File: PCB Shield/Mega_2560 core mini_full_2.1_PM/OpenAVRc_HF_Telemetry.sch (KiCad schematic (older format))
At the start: 14 parts, among them P18 Ecolage, P19 Module_TX, P20 TTL/RS232, P3 FTDI, P7 SPIX, U1 74LVC1G3157GV, U2 74LVC1G3157GV, U3 74LVC1G3157GV

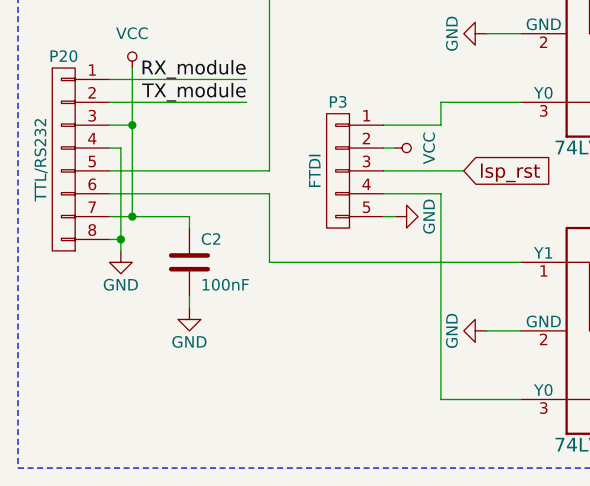
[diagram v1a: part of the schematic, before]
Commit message: Update schematic & pcb files
- modify pcb for haptic.
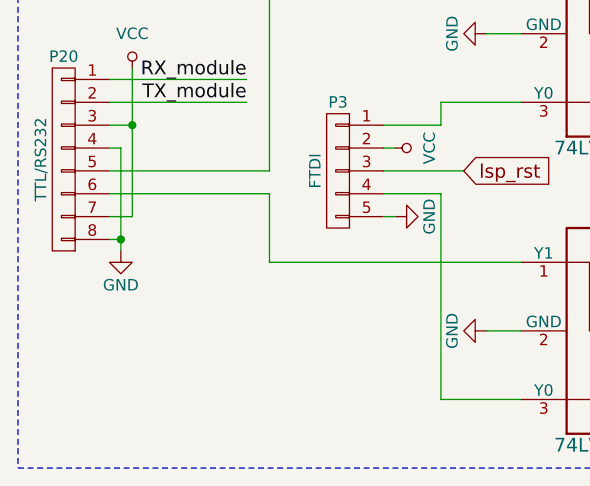
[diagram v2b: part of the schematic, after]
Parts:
- removed C2: 100nF, Capacitors_SMD:C_1206, symbol C-RESCUE-Mega_2560_core_mini_full_2.0
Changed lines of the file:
@@
 Sheet 4 7
 Title "Shield Mega2560 core Full"
-Date "2018-03-01"
+Date "2018-03-02"
 Rev "2.10"
 Comp "© Team OpenAVRc"
@@
 Wire Notes Line
 	4400 800  3250 800
-Wire Wire Line
-	1100 5200 1450 5200
 Wire Wire Line
 	1150 5300 1100 5300
@@
 Wire Wire Line
 	1800 5100 1100 5100
-$Comp
-L C-RESCUE-Mega_2560_core_mini_full_2.0 C2
-U 1 1 5A92C79D
-P 1450 5400
-F 0 "C2" H 1500 5500 50  0000 L CNN
-F 1 "100nF" H 1500 5300 50  0000 L CNN
-F 2 "Capacitors_SMD:C_1206" H 1488 5250 50  0001 C CNN
-F 3 "" H 1450 5400 50  0000 C CNN
-	1    1450 5400
-	1    0    0    -1
-$EndComp
-$Comp
-L GND-RESCUE-Mega_2560_core_mini_full_2.0 #PWR085
-U 1 1 5A92C7A3
-P 1450 5600
-F 0 "#PWR085" H 1450 5350 50  0001 C CNN
-F 1 "GND" H 1450 5450 50  0000 C CNN
-F 2 "" H 1450 5600 50  0000 C CNN
-F 3 "" H 1450 5600 50  0000 C CNN
-	1    1450 5600
-	1    0    0    -1
-$EndComp
-Wire Wire Line
-	1450 5600 1450 5550
-Wire Wire Line
-	1450 5200 1450 5250
-Connection ~ 1200 5200
 Wire Wire Line
 	2550 4700 2550 4800
@@
 Wire Wire Line
 	2900 5700 2750 5700
+Wire Wire Line
+	1200 5200 1100 5200
 $EndSCHEMATC

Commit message: Update schematic & pcb files
-remove P27.
-clean hold_power signal.
-add G3,H7 and G4 pins as dummy pins on 3 pins connector.
-update schematic.
-remove package errors in pcbnew.
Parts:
- P3: footprint (none) -> Pin_Header_Straight_1x05_Pitch2.54mm
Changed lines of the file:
@@
 Sheet 4 7
 Title "Shield Mega2560 core Full"
-Date "2018-03-02"
+Date "2018-03-06"
 Rev "2.10"
 Comp "© Team OpenAVRc"
@@
 F 0 "P3" H 2100 5300 50  0000 C CNN
 F 1 "FTDI" V 2200 5000 50  0000 C CNN
-F 2 "" H 2100 5000 50  0000 C CNN
+F 2 "Pin_Header_Straight_1x05_Pitch2.54mm" H 2100 5000 50  0001 C CNN
 F 3 "" H 2100 5000 50  0000 C CNN
 	1    2100 5000

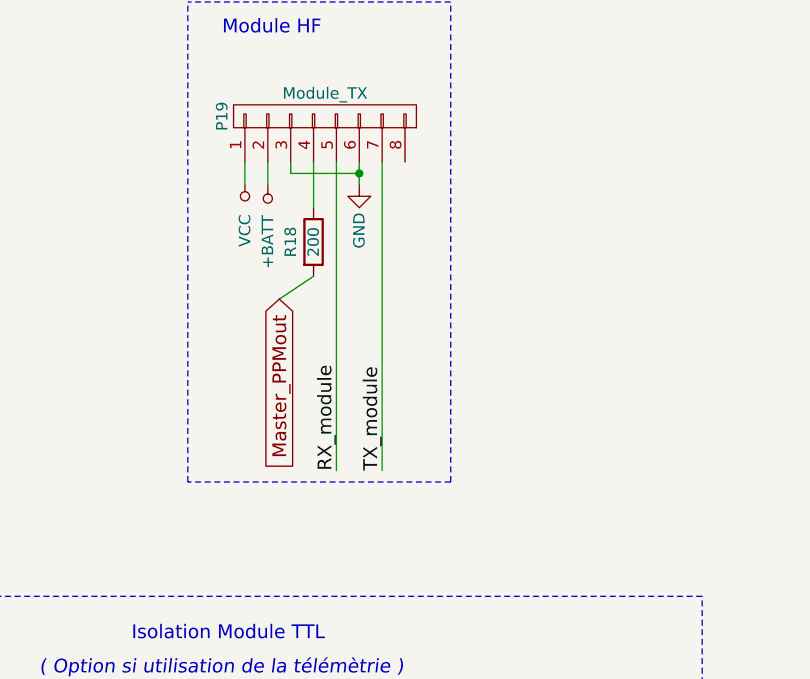
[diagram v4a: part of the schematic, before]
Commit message: Udpade shild v2.1
remove c10 on VREF and R21,R38 on I2C
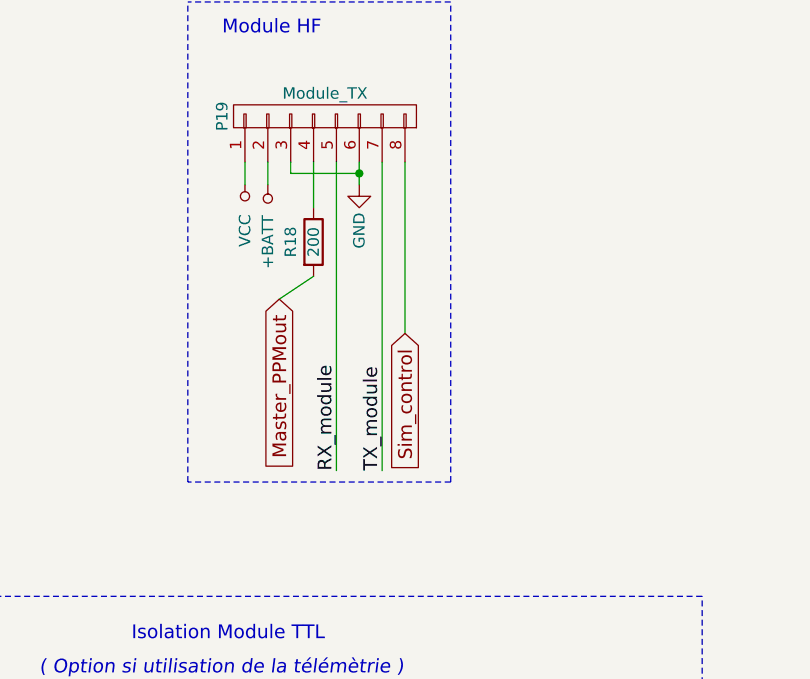
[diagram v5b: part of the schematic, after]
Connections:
- net Sim_control: now also P19.8 (P8)
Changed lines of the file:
@@
 Sheet 4 7
 Title "Shield Mega2560 core Full"
-Date "2018-03-16"
+Date "2018-04-19"
 Rev "2.10"
 Comp "© Team OpenAVRc"
@@
 $EndComp
 $Comp
-L GND-RESCUE-Mega_2560_core_mini_full_2.0 #PWR067
+L GND-RESCUE-Mega_2560_core_mini_full_2.0 #PWR066
 U 1 1 59C6B436
 P 4000 1600
-F 0 "#PWR067" H 4000 1350 50  0001 C CNN
+F 0 "#PWR066" H 4000 1350 50  0001 C CNN
 F 1 "GND" V 4000 1400 50  0000 C CNN
 F 2 "" H 4000 1600 50  0000 C CNN
@@
 $EndComp
 $Comp
-L VCC #PWR068
+L VCC #PWR067
 U 1 1 59C6B43D
 P 3500 1600
-F 0 "#PWR068" H 3500 1450 50  0001 C CNN
+F 0 "#PWR067" H 3500 1450 50  0001 C CNN
 F 1 "VCC" V 3500 1800 50  0000 C CNN
 F 2 "" H 3500 1600 50  0000 C CNN
@@
 Isolation Module TTL
 $Comp
-L +BATT #PWR069
+L +BATT #PWR068
 U 1 1 59C6B445
 P 3600 1600
-F 0 "#PWR069" H 3600 1450 50  0001 C CNN
+F 0 "#PWR068" H 3600 1450 50  0001 C CNN
 F 1 "+BATT" V 3600 1850 50  0000 C CNN
 F 2 "" H 3600 1600 50  0000 C CNN
@@
 $EndComp
 $Comp
-L GND-RESCUE-Mega_2560_core_mini_full_2.0 #PWR070
+L GND-RESCUE-Mega_2560_core_mini_full_2.0 #PWR069
 U 1 1 59C6B464
 P 9650 5100
-F 0 "#PWR070" H 9650 4850 50  0001 C CNN
+F 0 "#PWR069" H 9650 4850 50  0001 C CNN
 F 1 "GND" H 9650 4950 50  0000 C CNN
 F 2 "" H 9650 5100 50  0000 C CNN
@@
 $EndComp
 $Comp
-L GND-RESCUE-Mega_2560_core_mini_full_2.0 #PWR071
+L GND-RESCUE-Mega_2560_core_mini_full_2.0 #PWR070
 U 1 1 59C6B478
 P 1150 5350
-F 0 "#PWR071" H 1150 5100 50  0001 C CNN
+F 0 "#PWR070" H 1150 5100 50  0001 C CNN
 F 1 "GND" H 1150 5200 50  0000 C CNN
 F 2 "" H 1150 5350 50  0000 C CNN
@@
 $EndComp
 $Comp
-L VCC #PWR072
+L VCC #PWR071
 U 1 1 59C6B47E
 P 1200 4550
-F 0 "#PWR072" H 1200 4400 50  0001 C CNN
+F 0 "#PWR071" H 1200 4400 50  0001 C CNN
 F 1 "VCC" H 1200 4700 50  0000 C CNN
 F 2 "" H 1200 4550 50  0000 C CNN
@@
 $EndComp
 $Comp
-L VCC #PWR073
+L VCC #PWR072
 U 1 1 59C6B497
 P 8800 4500
-F 0 "#PWR073" H 8800 4350 50  0001 C CNN
+F 0 "#PWR072" H 8800 4350 50  0001 C CNN
 F 1 "VCC" H 8800 4650 50  0000 C CNN
 F 2 "" H 8800 4500 50  0000 C CNN
@@
 $EndComp
 $Comp
-L GND-RESCUE-Mega_2560_core_mini_full_2.0 #PWR074
+L GND-RESCUE-Mega_2560_core_mini_full_2.0 #PWR073
 U 1 1 59C6B49D
 P 7350 4500
-F 0 "#PWR074" H 7350 4250 50  0001 C CNN
+F 0 "#PWR073" H 7350 4250 50  0001 C CNN
 F 1 "GND" H 7350 4350 50  0000 C CNN
 F 2 "" H 7350 4500 50  0000 C CNN
@@
 $EndComp
 $Comp
-L GND-RESCUE-Mega_2560_core_mini_full_2.0 #PWR075
+L GND-RESCUE-Mega_2560_core_mini_full_2.0 #PWR074
 U 1 1 59C6C686
 P 7600 1800
-F 0 "#PWR075" H 7600 1550 50  0001 C CNN
+F 0 "#PWR074" H 7600 1550 50  0001 C CNN
 F 1 "GND" H 7600 1650 50  0000 C CNN
 F 2 "" H 7600 1800 50  0000 C CNN
@@
 $EndComp
 $Comp
-L GND-RESCUE-Mega_2560_core_mini_full_2.0 #PWR076
+L GND-RESCUE-Mega_2560_core_mini_full_2.0 #PWR075
 U 1 1 59C6C68C
 P 7300 1450
-F 0 "#PWR076" H 7300 1200 50  0001 C CNN
+F 0 "#PWR075" H 7300 1200 50  0001 C CNN
 F 1 "GND" H 7300 1300 50  0000 C CNN
 F 2 "" H 7300 1450 50  0000 C CNN
@@
 $EndComp
 $Comp
-L VCC #PWR077
+L VCC #PWR076
 U 1 1 59C6C694
 P 7400 1600
-F 0 "#PWR077" H 7400 1450 50  0001 C CNN
+F 0 "#PWR076" H 7400 1450 50  0001 C CNN
 F 1 "VCC" V 7400 1750 50  0000 C CNN
 F 2 "" H 7400 1600 50  0000 C CNN
@@
 Sim_control
 $Comp
-L +3,3V #PWR078
+L +3,3V #PWR077
 U 1 1 59CA7757
 P 7100 1550
-F 0 "#PWR078" H 7100 1510 30  0001 C CNN
+F 0 "#PWR077" H 7100 1510 30  0001 C CNN
 F 1 "+3,3V" V 7100 1750 39  0000 C CNN
 F 2 "" H 7100 1550 60  0001 C CNN
@@
 $EndComp
 $Comp
-L VCC #PWR079
+L VCC #PWR078
 U 1 1 5A92799A
 P 4100 4400
-F 0 "#PWR079" H 4100 4250 50  0001 C CNN
+F 0 "#PWR078" H 4100 4250 50  0001 C CNN
 F 1 "VCC" H 4100 4550 50  0000 C CNN
 F 2 "" H 4100 4400 50  0000 C CNN
@@
 	3900 4400 4100 4400
 $Comp
-L VCC #PWR080
+L VCC #PWR079
 U 1 1 5A9279BB
 P 4100 5700
-F 0 "#PWR080" H 4100 5550 50  0001 C CNN
+F 0 "#PWR079" H 4100 5550 50  0001 C CNN
 F 1 "VCC" H 4100 5850 50  0000 C CNN
 F 2 "" H 4100 5700 50  0000 C CNN
@@
 	3900 5700 4100 5700
 $Comp
-L GND-RESCUE-Mega_2560_core_mini_full_2.0 #PWR081
+L GND-RESCUE-Mega_2560_core_mini_full_2.0 #PWR080
 U 1 1 5A9279DC
 P 2750 4400
-F 0 "#PWR081" H 2750 4150 50  0001 C CNN
+F 0 "#PWR080" H 2750 4150 50  0001 C CNN
 F 1 "GND" H 2750 4250 50  0000 C CNN
 F 2 "" H 2750 4400 50  0000 C CNN
@@
 	2900 4400 2750 4400
 $Comp
-L GND-RESCUE-Mega_2560_core_mini_full_2.0 #PWR082
+L GND-RESCUE-Mega_2560_core_mini_full_2.0 #PWR081
 U 1 1 5A9279FD
 P 2750 5700
-F 0 "#PWR082" H 2750 5450 50  0001 C CNN
+F 0 "#PWR081" H 2750 5450 50  0001 C CNN
 F 1 "GND" H 2750 5550 50  0000 C CNN
 F 2 "" H 2750 5700 50  0000 C CNN
@@
 $EndComp
 $Comp
-L VCC #PWR083
+L VCC #PWR082
 U 1 1 5A92837D
 P 2350 4900
-F 0 "#PWR083" H 2350 4750 50  0001 C CNN
+F 0 "#PWR082" H 2350 4750 50  0001 C CNN
 F 1 "VCC" H 2350 5050 50  0000 C CNN
 F 2 "" H 2350 4900 50  0000 C CNN
@@
 $EndComp
 $Comp
-L GND-RESCUE-Mega_2560_core_mini_full_2.0 #PWR084
+L GND-RESCUE-Mega_2560_core_mini_full_2.0 #PWR083
 U 1 1 5A9283AC
 P 2350 5200
-F 0 "#PWR084" H 2350 4950 50  0001 C CNN
+F 0 "#PWR083" H 2350 4950 50  0001 C CNN
 F 1 "GND" H 2350 5050 50  0000 C CNN
 F 2 "" H 2350 5200 50  0000 C CNN
@@
 Wire Wire Line
 	1200 5200 1100 5200
+Text GLabel 4200 2250 3    60   Input ~ 0
+Sim_control
+Wire Wire Line
+	4200 2250 4200 1500
 $EndSCHEMATC

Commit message: Update pcb shield
Update core component (change pin 99 from GND to AGND).
Remove GND on AGND pin.
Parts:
- P3: footprint Pin_Header_Straight_1x05_Pitch2.54mm -> v2.1:Pin_Header_Straight_1x05_Pitch2.54mm
- U1, U2, U3: footprint SOT-457 -> v2.1:SOT-457
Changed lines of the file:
@@
 Sheet 4 7
 Title "Shield Mega2560 core Full"
-Date "2018-04-19"
+Date "2018-04-25"
 Rev "2.10"
 Comp "© Team OpenAVRc"
@@
 $EndComp
 $Comp
-L GND-RESCUE-Mega_2560_core_mini_full_2.0 #PWR066
+L GND-RESCUE-Mega_2560_core_mini_full_2.0 #PWR067
 U 1 1 59C6B436
 P 4000 1600
-F 0 "#PWR066" H 4000 1350 50  0001 C CNN
+F 0 "#PWR067" H 4000 1350 50  0001 C CNN
 F 1 "GND" V 4000 1400 50  0000 C CNN
 F 2 "" H 4000 1600 50  0000 C CNN
@@
 $EndComp
 $Comp
-L VCC #PWR067
+L VCC #PWR068
 U 1 1 59C6B43D
 P 3500 1600
-F 0 "#PWR067" H 3500 1450 50  0001 C CNN
+F 0 "#PWR068" H 3500 1450 50  0001 C CNN
 F 1 "VCC" V 3500 1800 50  0000 C CNN
 F 2 "" H 3500 1600 50  0000 C CNN
@@
 Isolation Module TTL
 $Comp
-L +BATT #PWR068
+L +BATT #PWR069
 U 1 1 59C6B445
 P 3600 1600
-F 0 "#PWR068" H 3600 1450 50  0001 C CNN
+F 0 "#PWR069" H 3600 1450 50  0001 C CNN
 F 1 "+BATT" V 3600 1850 50  0000 C CNN
 F 2 "" H 3600 1600 50  0000 C CNN
@@
 $EndComp
 $Comp
-L GND-RESCUE-Mega_2560_core_mini_full_2.0 #PWR069
+L GND-RESCUE-Mega_2560_core_mini_full_2.0 #PWR070
 U 1 1 59C6B464
 P 9650 5100
-F 0 "#PWR069" H 9650 4850 50  0001 C CNN
+F 0 "#PWR070" H 9650 4850 50  0001 C CNN
 F 1 "GND" H 9650 4950 50  0000 C CNN
 F 2 "" H 9650 5100 50  0000 C CNN
@@
 $EndComp
 $Comp
-L GND-RESCUE-Mega_2560_core_mini_full_2.0 #PWR070
+L GND-RESCUE-Mega_2560_core_mini_full_2.0 #PWR071
 U 1 1 59C6B478
 P 1150 5350
-F 0 "#PWR070" H 1150 5100 50  0001 C CNN
+F 0 "#PWR071" H 1150 5100 50  0001 C CNN
 F 1 "GND" H 1150 5200 50  0000 C CNN
 F 2 "" H 1150 5350 50  0000 C CNN
@@
 $EndComp
 $Comp
-L VCC #PWR071
+L VCC #PWR072
 U 1 1 59C6B47E
 P 1200 4550
-F 0 "#PWR071" H 1200 4400 50  0001 C CNN
+F 0 "#PWR072" H 1200 4400 50  0001 C CNN
 F 1 "VCC" H 1200 4700 50  0000 C CNN
 F 2 "" H 1200 4550 50  0000 C CNN
@@
 F 0 "U1" H 8100 5050 60  0000 C CNN
 F 1 "74LVC1G3157GV" H 8100 4000 60  0000 C CNN
-F 2 "SOT-457" H 8100 4500 60  0001 C CNN
+F 2 "v2.1:SOT-457" H 8100 4500 60  0001 C CNN
 F 3 "" H 8100 4500 60  0000 C CNN
 	1    8100 4500
@@
 $EndComp
 $Comp
-L VCC #PWR072
+L VCC #PWR073
 U 1 1 59C6B497
 P 8800 4500
-F 0 "#PWR072" H 8800 4350 50  0001 C CNN
+F 0 "#PWR073" H 8800 4350 50  0001 C CNN
 F 1 "VCC" H 8800 4650 50  0000 C CNN
 F 2 "" H 8800 4500 50  0000 C CNN
@@
 $EndComp
 $Comp
-L GND-RESCUE-Mega_2560_core_mini_full_2.0 #PWR073
+L GND-RESCUE-Mega_2560_core_mini_full_2.0 #PWR074
 U 1 1 59C6B49D
 P 7350 4500
-F 0 "#PWR073" H 7350 4250 50  0001 C CNN
+F 0 "#PWR074" H 7350 4250 50  0001 C CNN
 F 1 "GND" H 7350 4350 50  0000 C CNN
 F 2 "" H 7350 4500 50  0000 C CNN
@@
 $EndComp
 $Comp
-L GND-RESCUE-Mega_2560_core_mini_full_2.0 #PWR074
+L GND-RESCUE-Mega_2560_core_mini_full_2.0 #PWR075
 U 1 1 59C6C686
 P 7600 1800
-F 0 "#PWR074" H 7600 1550 50  0001 C CNN
+F 0 "#PWR075" H 7600 1550 50  0001 C CNN
 F 1 "GND" H 7600 1650 50  0000 C CNN
 F 2 "" H 7600 1800 50  0000 C CNN
@@
 $EndComp
 $Comp
-L GND-RESCUE-Mega_2560_core_mini_full_2.0 #PWR075
+L GND-RESCUE-Mega_2560_core_mini_full_2.0 #PWR076
 U 1 1 59C6C68C
 P 7300 1450
-F 0 "#PWR075" H 7300 1200 50  0001 C CNN
+F 0 "#PWR076" H 7300 1200 50  0001 C CNN
 F 1 "GND" H 7300 1300 50  0000 C CNN
 F 2 "" H 7300 1450 50  0000 C CNN
@@
 $EndComp
 $Comp
-L VCC #PWR076
+L VCC #PWR077
 U 1 1 59C6C694
 P 7400 1600
-F 0 "#PWR076" H 7400 1450 50  0001 C CNN
+F 0 "#PWR077" H 7400 1450 50  0001 C CNN
 F 1 "VCC" V 7400 1750 50  0000 C CNN
 F 2 "" H 7400 1600 50  0000 C CNN
@@
 Sim_control
 $Comp
-L +3,3V #PWR077
+L +3,3V #PWR078
 U 1 1 59CA7757
 P 7100 1550
-F 0 "#PWR077" H 7100 1510 30  0001 C CNN
+F 0 "#PWR078" H 7100 1510 30  0001 C CNN
 F 1 "+3,3V" V 7100 1750 39  0000 C CNN
 F 2 "" H 7100 1550 60  0001 C CNN
@@
 F 0 "U2" H 3400 4950 60  0000 C CNN
 F 1 "74LVC1G3157GV" H 3400 3900 60  0000 C CNN
-F 2 "SOT-457" H 3400 4400 60  0001 C CNN
+F 2 "v2.1:SOT-457" H 3400 4400 60  0001 C CNN
 F 3 "" H 3400 4400 60  0000 C CNN
 	1    3400 4400
@@
 F 0 "U3" H 3400 6250 60  0000 C CNN
 F 1 "74LVC1G3157GV" H 3400 5200 60  0000 C CNN
-F 2 "SOT-457" H 3400 5700 60  0001 C CNN
+F 2 "v2.1:SOT-457" H 3400 5700 60  0001 C CNN
 F 3 "" H 3400 5700 60  0000 C CNN
 	1    3400 5700
@@
 $EndComp
 $Comp
-L VCC #PWR078
+L VCC #PWR079
 U 1 1 5A92799A
 P 4100 4400
-F 0 "#PWR078" H 4100 4250 50  0001 C CNN
+F 0 "#PWR079" H 4100 4250 50  0001 C CNN
 F 1 "VCC" H 4100 4550 50  0000 C CNN
 F 2 "" H 4100 4400 50  0000 C CNN
@@
 	3900 4400 4100 4400
 $Comp
-L VCC #PWR079
+L VCC #PWR080
 U 1 1 5A9279BB
 P 4100 5700
-F 0 "#PWR079" H 4100 5550 50  0001 C CNN
+F 0 "#PWR080" H 4100 5550 50  0001 C CNN
 F 1 "VCC" H 4100 5850 50  0000 C CNN
 F 2 "" H 4100 5700 50  0000 C CNN
@@
 	3900 5700 4100 5700
 $Comp
-L GND-RESCUE-Mega_2560_core_mini_full_2.0 #PWR080
+L GND-RESCUE-Mega_2560_core_mini_full_2.0 #PWR081
 U 1 1 5A9279DC
 P 2750 4400
-F 0 "#PWR080" H 2750 4150 50  0001 C CNN
+F 0 "#PWR081" H 2750 4150 50  0001 C CNN
 F 1 "GND" H 2750 4250 50  0000 C CNN
 F 2 "" H 2750 4400 50  0000 C CNN
@@
 	2900 4400 2750 4400
 $Comp
-L GND-RESCUE-Mega_2560_core_mini_full_2.0 #PWR081
+L GND-RESCUE-Mega_2560_core_mini_full_2.0 #PWR082
 U 1 1 5A9279FD
 P 2750 5700
-F 0 "#PWR081" H 2750 5450 50  0001 C CNN
+F 0 "#PWR082" H 2750 5450 50  0001 C CNN
 F 1 "GND" H 2750 5550 50  0000 C CNN
 F 2 "" H 2750 5700 50  0000 C CNN
@@
 F 0 "P3" H 2100 5300 50  0000 C CNN
 F 1 "FTDI" V 2200 5000 50  0000 C CNN
-F 2 "Pin_Header_Straight_1x05_Pitch2.54mm" H 2100 5000 50  0001 C CNN
+F 2 "v2.1:Pin_Header_Straight_1x05_Pitch2.54mm" H 2100 5000 50  0001 C CNN
 F 3 "" H 2100 5000 50  0000 C CNN
 	1    2100 5000
@@
 $EndComp
 $Comp
-L VCC #PWR082
+L VCC #PWR083
 U 1 1 5A92837D
 P 2350 4900
-F 0 "#PWR082" H 2350 4750 50  0001 C CNN
+F 0 "#PWR083" H 2350 4750 50  0001 C CNN
 F 1 "VCC" H 2350 5050 50  0000 C CNN
 F 2 "" H 2350 4900 50  0000 C CNN
@@
 $EndComp
 $Comp
-L GND-RESCUE-Mega_2560_core_mini_full_2.0 #PWR083
+L GND-RESCUE-Mega_2560_core_mini_full_2.0 #PWR084
 U 1 1 5A9283AC
 P 2350 5200
-F 0 "#PWR083" H 2350 4950 50  0001 C CNN
+F 0 "#PWR084" H 2350 4950 50  0001 C CNN
 F 1 "GND" H 2350 5050 50  0000 C CNN
 F 2 "" H 2350 5200 50  0000 C CNN
